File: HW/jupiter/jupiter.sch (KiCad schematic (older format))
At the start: 0 parts

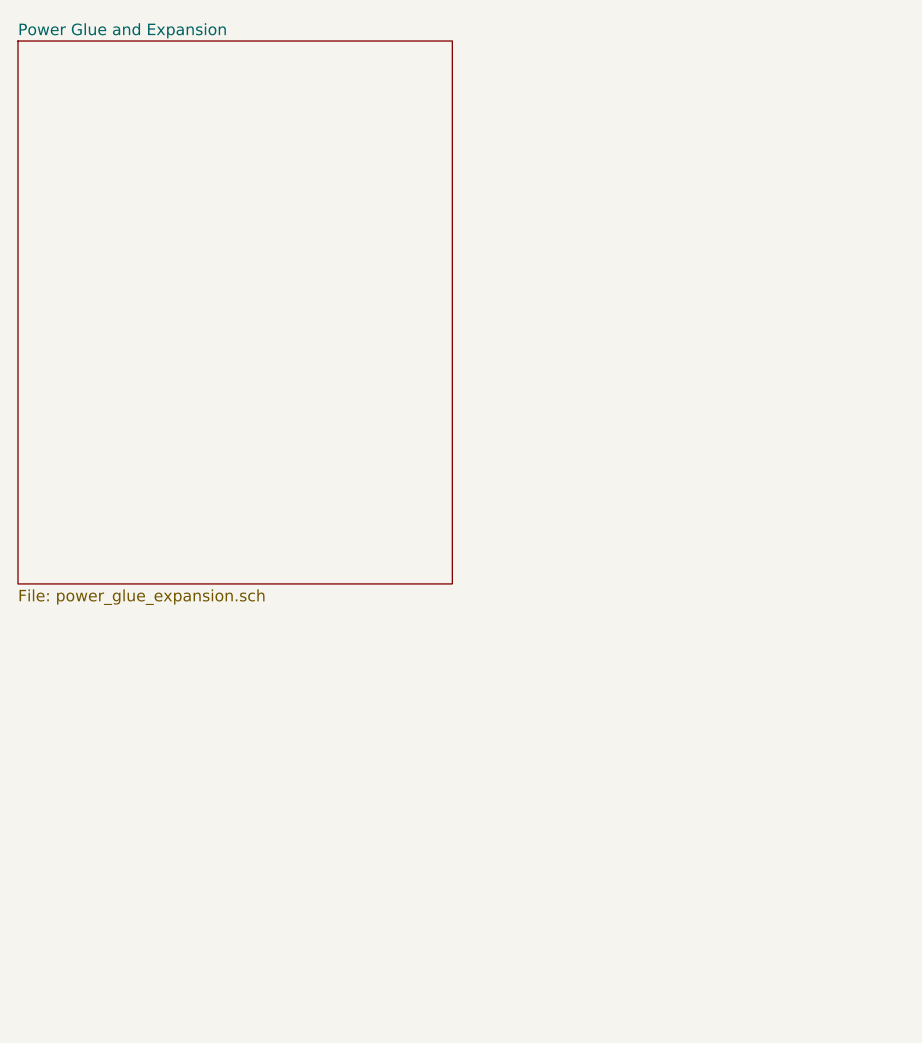
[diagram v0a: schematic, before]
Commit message: Schematics to clock, reset, panic and power section done.
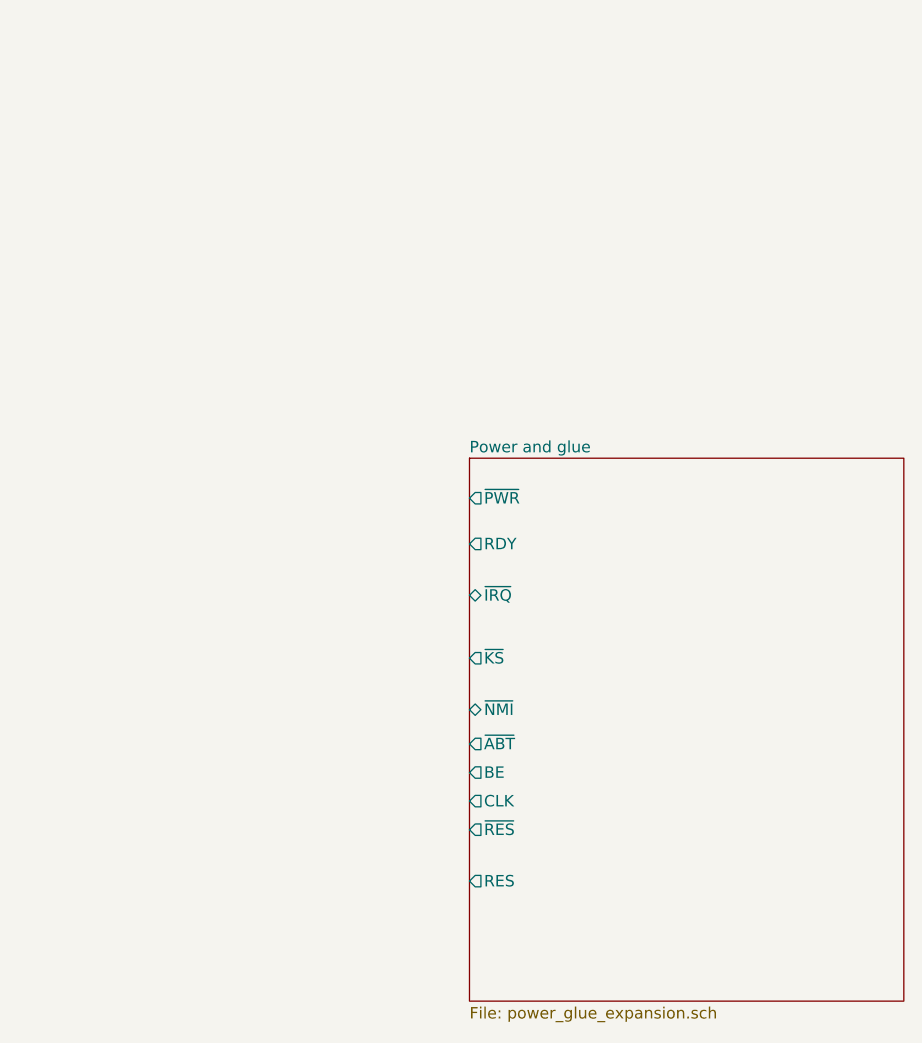
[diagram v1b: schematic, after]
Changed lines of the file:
@@
 $EndDescr
 $Sheet
-S 2275 1725 1900 2375
+S 4250 3550 1900 2375
 U 5D10A452
-F0 "Power Glue and Expansion" 50
+F0 "Power and glue" 50
 F1 "power_glue_expansion.sch" 50
+F2 "~KS" O L 4250 4425 50
+F3 "~IRQ" B L 4250 4150 50
+F4 "~NMI" B L 4250 4650 50
+F5 "BE" O L 4250 4925 50
+F6 "RDY" O L 4250 3925 50
+F7 "~ABT" O L 4250 4800 50
+F8 "~PWR" O L 4250 3725 50
+F9 "~RES" O L 4250 5175 50
+F10 "RES" O L 4250 5400 50
+F11 "CLK" O L 4250 5050 50
 $EndSheet
 $EndSCHEMATC
